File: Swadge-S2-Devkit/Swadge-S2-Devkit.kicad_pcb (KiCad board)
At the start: 2 copper layers, 167.6 x 101.6 mm, 72 parts, among them J5 MICSEL, J6 TRYMIC, J7 LEDK_J, J8 LCD18, J9 LCD28, P1 USB_C_Plug_USB2.0, Q4 AP2003_PN_FET, SW1 EVQ-Q2B03W, SW2 EVQ-Q2B03W, SW3 EVQ-Q2B03W, SW4 EVQ-Q2B03W, SW5 EVQ-Q2B03W, SW6 EVQ-Q2B03W, SW7 SW_SPDT_1825232-1, SW8 logo_start_select, U1 ESP32-S2-SOLO, U10 GENERIC_LDO_2.8, U11 LCD_240x240_1.3_12, U12 LCD_135x240_1.14_13, U15 LCD_240x240_1.54_12, U3 MT3410, U4 GS321-TR, U9 GENERIC_LDO_1.8

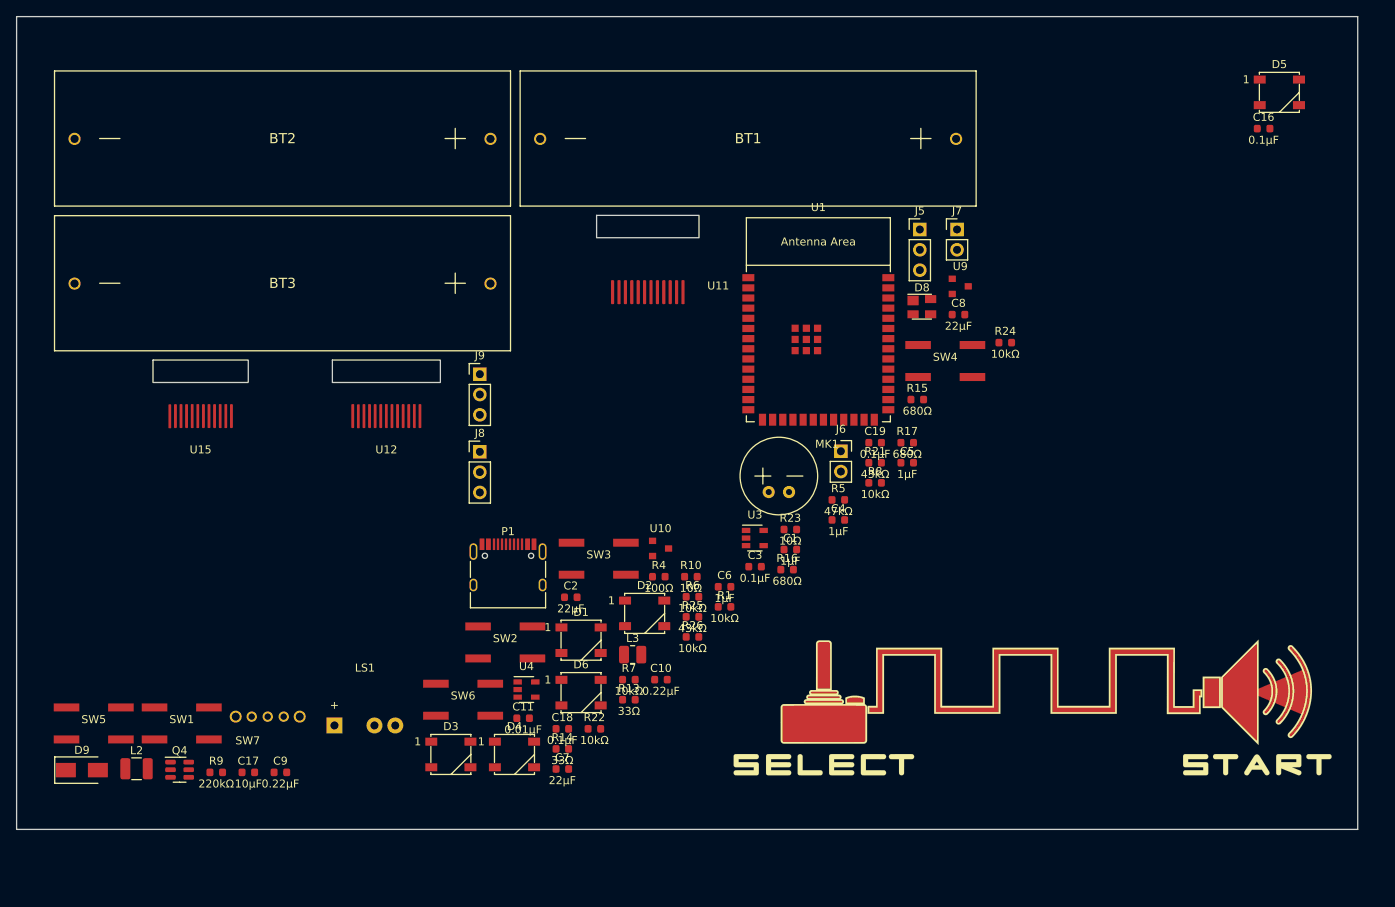
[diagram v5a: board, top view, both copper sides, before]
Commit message: Updated buttons, LEDs, TFTs for prototype
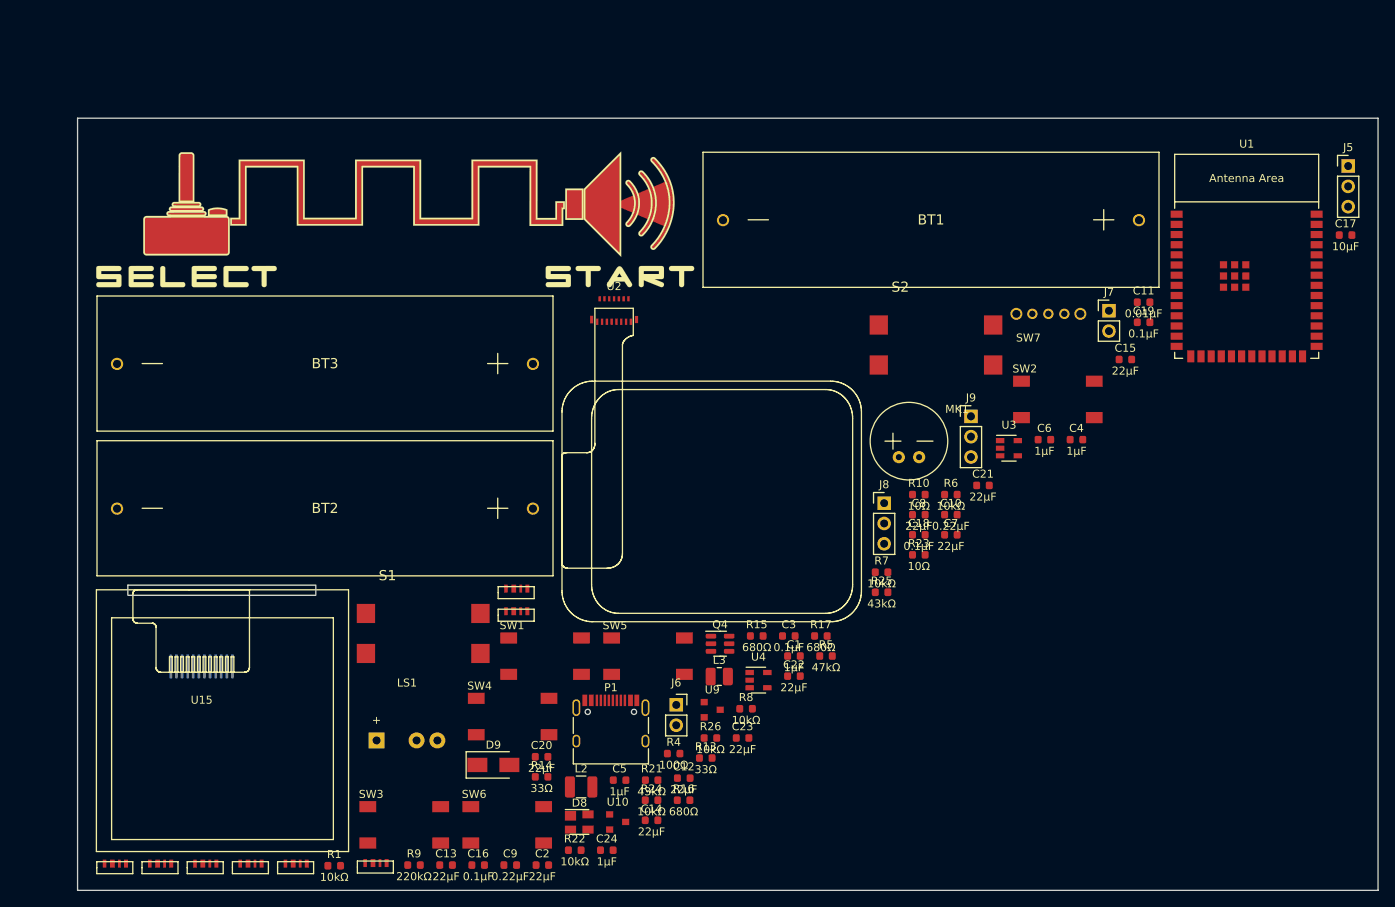
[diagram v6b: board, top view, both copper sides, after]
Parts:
- removed U11: LCD_240x240_1.3_12, Swadge_Parts:LCD_240x240_1.3_12
- removed U12: LCD_135x240_1.14_13, Swadge_Parts:LCD_135x240_1.14_13
- added C12: 22μF, Swadge_Parts:C_0603_1608Metric, F.Cu at (144.5, 134.2)
- added C13: 22μF, Swadge_Parts:C_0603_1608Metric, F.Cu at (114.8, 145.1)
- added C14: 22μF, Swadge_Parts:C_0603_1608Metric, F.Cu at (140.5, 139.5)
- added C15: 22μF, Swadge_Parts:C_0603_1608Metric, F.Cu at (199.7, 81.9)
- added C20: 22μF, Swadge_Parts:C_0603_1608Metric, F.Cu at (126.7, 131.6)
- added C21: 22μF, Swadge_Parts:C_0603_1608Metric, F.Cu at (181.9, 97.6)
- added C22: 22μF, Swadge_Parts:C_0603_1608Metric, F.Cu at (158.3, 121.5)
- added C23: 22μF, Swadge_Parts:C_0603_1608Metric, F.Cu at (151.8, 129.2)
- added C24: 1μF, Swadge_Parts:C_0603_1608Metric, F.Cu at (134.9, 143.2)
- added D10: SK6812SIDE, Swadge_Parts:SK6812SIDE, F.Cu at (123.5, 113.9)
- added D7: SK6812SIDE, Swadge_Parts:SK6812SIDE, F.Cu at (96.0, 145.4)
- added S1: B3FS-4002P, Swadge_Parts:B3FS4002P, F.Cu at (113.0, 116.1)
- added S2: B3FS-4002P, Swadge_Parts:B3FS4002P, F.Cu at (177.1, 80.1)
- added U2: RB017A1505A, Swadge_Parts:FH26W-15S-0.3SHW(60), F.Cu at (135.8, 75.7)
- D1, D2, D3, D4, D5, D6: value WS2812B -> SK6812SIDE; footprint Swadge_Parts:LED_WS2812B_PLCC4_5.0x5.0mm_P3.2mm -> Swadge_Parts:SK6812SIDE
- SW1, SW2, SW3, SW4, SW5, SW6: value EVQ-Q2B03W -> TS-1109S-A-A; footprint Swadge_Parts:EVQ-Q2B03W -> Swadge_Parts:SW_4-1437565-2
- moved C17 152.7 mm to (227.2, 66.3)
- moved D5 148.8 mm to (105.9, 145.3)
- moved C16 134.6 mm to (118.8, 145.1)
- moved SW7 109.8 mm to (190.1, 76.2)
- moved SW8 100.4 mm to (108.4, 64.4)
- moved C11 93.4 mm to (202.0, 74.7)
- moved D8 77.3 mm to (131.4, 139.7)
- moved SW2 75.5 mm to (191.3, 86.9)
- moved R24 72.3 mm to (140.5, 137.0)
- moved SW4 70.0 mm to (123.1, 126.5)
- moved SW5 69.8 mm to (140.0, 119.0)
- moved Q4 69.4 mm to (149.0, 117.4)
- moved J9 61.6 mm to (180.4, 89.0)
- moved U9 61.3 mm to (148.1, 125.7)
- moved D1 59.8 mm to (79.0, 145.4)
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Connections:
- D1 pad 1: +3V3 -> Net-(R4-Pad2)
- D1 pad 2: Net-(D1-Pad2) -> +3V3
- D1 pad 3: GND -> Net-(D1-Pad3)
- D1 pad 4: Net-(D1-Pad4) -> GND
- D2 pad 1: +3V3 -> Net-(D1-Pad3)
- D2 pad 2: Net-(D2-Pad2) -> +3V3
- D2 pad 3: GND -> Net-(D2-Pad3)
- D2 pad 4: Net-(D1-Pad2) -> GND
- D3 pad 1: +3V3 -> Net-(D2-Pad3)
- D3 pad 2: Net-(D3-Pad2) -> +3V3
- D3 pad 3: GND -> Net-(D3-Pad3)
- D3 pad 4: Net-(D2-Pad2) -> GND
- D4 pad 1: +3V3 -> Net-(D3-Pad3)
- D4 pad 2: Net-(D4-Pad2) -> +3V3
- D4 pad 3: GND -> Net-(D4-Pad3)
- D4 pad 4: Net-(D3-Pad2) -> GND
- D5 pad 1: +3V3 -> Net-(D4-Pad3)
- D5 pad 2: Net-(D5-Pad2) -> +3V3
- D5 pad 3: GND -> Net-(D5-Pad3)
- D5 pad 4: Net-(D4-Pad2) -> GND
- D6 pad 1: +3V3 -> Net-(D5-Pad3)
- D6 pad 2: LED_OUT -> +3V3
- D6 pad 3: GND -> Net-(D6-Pad3)
- D6 pad 4: Net-(D5-Pad2) -> GND
- R4 pad 1: Net-(D1-Pad4) -> LED
- R4 pad 2: LED -> Net-(R4-Pad2)
- U1 pad 15: BTN_4 -> unconnected-(U1-Pad15)
- U1 pad 22: unconnected-(U1-Pad22) -> TFT_FMARK
- U1 pad 4: BTN_5 -> BTN_4
- U1 pad 5: BTN_6 -> BTN_5
- U1 pad 7: unconnected-(U1-Pad7) -> BTN_6
- U1 pad 8: unconnected-(U1-Pad8) -> BTN_7
- U1 pad 9: unconnected-(U1-Pad9) -> BTN_8
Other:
- board size 167.6 x 101.6 mm -> 162.6 x 96.5 mm

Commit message: Started prototype part placement
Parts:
- removed SW8: logo_start_select, Swadge_Parts:start_select
- added Ref**: Val**, Swadge_Parts:Controller_Shape, F.Cu at (150.0, 100.0)
- added U11: art_melee_logo, Swadge_Parts:Melee_Logo, F.Cu at (101.7, 105.1)
- added U12: art_select_start, Swadge_Parts:select-start, F.Cu at (150.0, 87.3)
- added U13: art_squarewavebird, Swadge_Parts:squarewavebird, F.Cu at (150.0, 133.0)
- added U5: art_xy_buttons, Swadge_Parts:XY_Buttons, F.Cu at (189.4, 69.5)
- added U6: art_20th_logo, Swadge_Parts:20th_Logo, F.Cu at (198.3, 105.1)
- added U7: art_d_pad, Swadge_Parts:d-pad, F.Cu at (110.6, 81.2)
- added U8: art_eyebrow, Swadge_Parts:eyebrow, F.Cu at (139.8, 67.0)
- BT1, BT2, BT3, P1, SW7, U1: moved to B.Cu
- moved C19 235.6 mm to (-16.2, -11.6)
- moved U9 224.1 mm to (67.7, -83.5)
- moved D4 223.0 mm to (29.1, -70.6)
- moved D1 220.5 mm to (34.8, -70.6)
- moved R23 215.1 mm to (3.29, -24.8)
- moved D8 207.0 mm to (35.5, -43.7)
- moved D9 206.3 mm to (-27.9, -10.6)
- moved L2 206.0 mm to (30.1, -43.9)
- moved J5 204.2 mm to (43.2, -30.0)
- moved C1 202.8 mm to (0.76, -8.74)
- moved D5 199.5 mm to (-21.0, -8.57)
- moved C2 196.7 mm to (96.6, -49.2)
- moved R17 196.4 mm to (11.0, -9.48)
- moved R24 195.0 mm to (55.7, -38.6)
- moved D2 193.2 mm to (-1.54, -24.5)
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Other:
- board size 162.6 x 96.5 mm -> 131.2 x 95.7 mm
